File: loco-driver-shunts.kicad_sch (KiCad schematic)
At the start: 0 parts

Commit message: Fix - ERC updates
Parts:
- added R101: 1k, symbol Device:R
- added R102: 1k5, symbol Device:R
- added R103: 39k, symbol Device:R
- added U101: LMV393, symbol Comparator:LMV393
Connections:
- net GND: now also R101.2, U101.4 (V-)
- net I_FUNC: now also U101.5 (+)
- net I_MOTOR: now also U101.3 (+)
- new net +3V3: R103.1, U101.8 (V+)
- new net 200mV: R102.1, R103.2, U101.2 (-)
- new net 80mV: R101.1, R102.2, U101.6 (-)
- new net OFF_ MOTOR: U101.1
- new net OFF_FUNC: U101.7

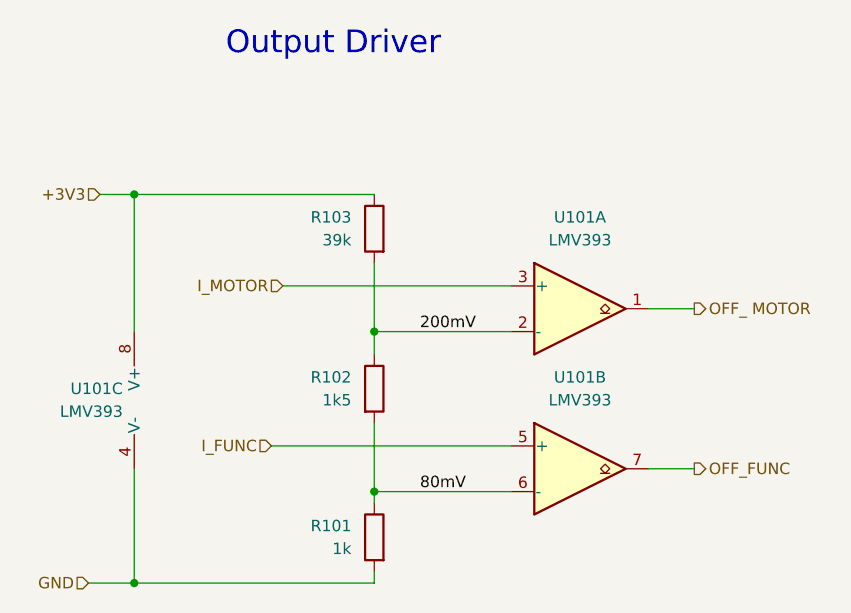
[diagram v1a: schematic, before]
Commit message: Fix - Ignore double power flags
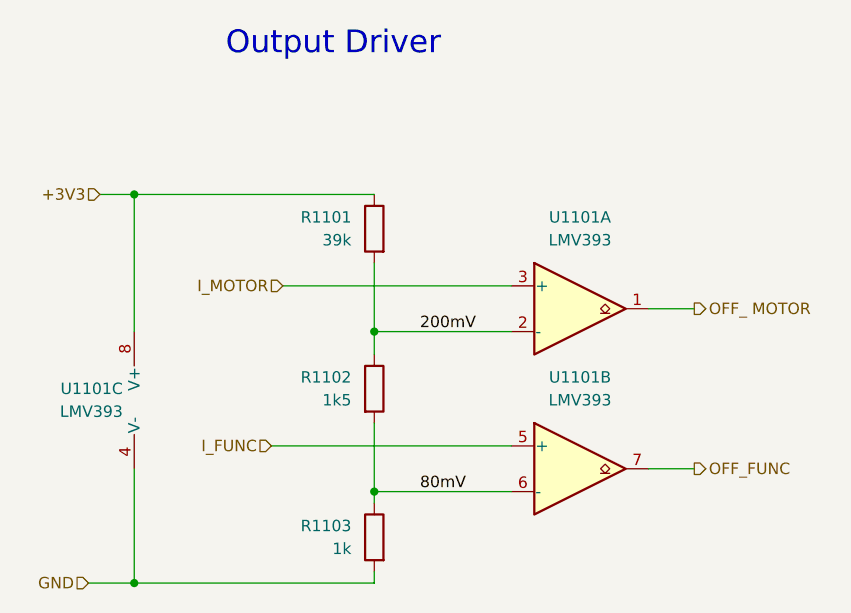
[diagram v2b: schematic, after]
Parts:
- renumbered R103 to R1101, R102 to R1102, R101 to R1103, U101 to U1101
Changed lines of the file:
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@@
 		(dnp no)
 		(fields_autoplaced yes)
-		(property "Reference" "U101"
+		(property "Reference" "U1101"
 			(at 34.29 58.4199 0)
 			(effects
@@
 			(project ""
 				(path "/fb33ec4e-6596-45d2-a121-8d3475acd69a/a9403bde-50df-4cf0-b8d0-25b03e0e0cbd"
-					(reference "U101")
+					(reference "U1101")
 					(unit 3)
 				)
@@
 		(on_board yes)
 		(dnp no)
-		(property "Reference" "R103"
+		(property "Reference" "R1101"
 			(at 59.69 39.3699 0)
 			(effects
@@
 			(project "xDuinoRails-Thor-M"
 				(path "/fb33ec4e-6596-45d2-a121-8d3475acd69a/a9403bde-50df-4cf0-b8d0-25b03e0e0cbd"
-					(reference "R103")
+					(reference "R1101")
 					(unit 1)
 				)
@@
 		(on_board yes)
 		(dnp no)
-		(property "Reference" "U101"
+		(property "Reference" "U1101"
 			(at 85.09 39.37 0)
 			(effects
@@
 			(project ""
 				(path "/fb33ec4e-6596-45d2-a121-8d3475acd69a/a9403bde-50df-4cf0-b8d0-25b03e0e0cbd"
-					(reference "U101")
+					(reference "U1101")
 					(unit 1)
 				)
@@
 		(dnp no)
 		(fields_autoplaced yes)
-		(property "Reference" "R101"
+		(property "Reference" "R1103"
 			(at 59.69 73.6599 0)
 			(effects
@@
 			(project ""
 				(path "/fb33ec4e-6596-45d2-a121-8d3475acd69a/a9403bde-50df-4cf0-b8d0-25b03e0e0cbd"
-					(reference "R101")
+					(reference "R1103")
 					(unit 1)
 				)
@@
 		(dnp no)
 		(fields_autoplaced yes)
-		(property "Reference" "U101"
+		(property "Reference" "U1101"
 			(at 85.09 57.15 0)
 			(effects
@@
 			(project ""
 				(path "/fb33ec4e-6596-45d2-a121-8d3475acd69a/a9403bde-50df-4cf0-b8d0-25b03e0e0cbd"
-					(reference "U101")
+					(reference "U1101")
 					(unit 2)
 				)
@@
 		(on_board yes)
 		(dnp no)
-		(property "Reference" "R102"
+		(property "Reference" "R1102"
 			(at 59.69 57.1499 0)
 			(effects
@@
 			(project "xDuinoRails-Thor-M"
 				(path "/fb33ec4e-6596-45d2-a121-8d3475acd69a/a9403bde-50df-4cf0-b8d0-25b03e0e0cbd"
-					(reference "R102")
+					(reference "R1102")
 					(unit 1)
 				)
